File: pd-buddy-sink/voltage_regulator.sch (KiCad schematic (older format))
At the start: 5 parts, among them U1 AP2204R-3.3

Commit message: Added test points, replaced SW1 with R11
More test points will be needed for automated testing, so I've added the
first two I know of.

With firmware version 1.2.0+, there's not much reason to install SW1
anymore.  This commit replaces it with R11, an unpopulated resistor
footprint that does the same thing as bridging the two pins of SW1 used
to do, just in case an upgrade make the `boot` command stop working.
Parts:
- TP1, TP2: symbol TEST -> Test_Point
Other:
- moved on the sheet: TP1, TP2
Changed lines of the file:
@@
 $EndComp
 $Comp
-L TEST TP1
+L Test_Point TP1
 U 1 1 58FBCF4C
 P 4600 3600
@@
 $EndComp
 $Comp
-L TEST TP2
+L Test_Point TP2
 U 1 1 58FBD023
 P 4600 3800

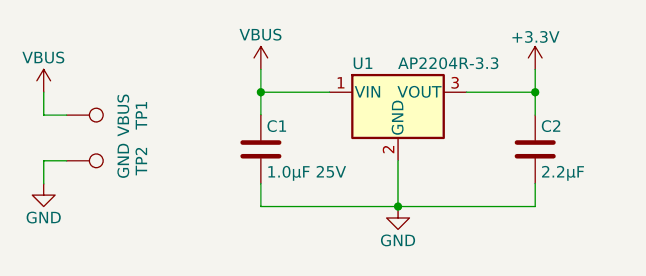
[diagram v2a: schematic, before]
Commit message: Update to KiCad 5.0 nightly
Hooray, new stuff!  The STM32 symbol is a reasonable size now!  We have
a sym-lib-table!  Everything is great, and I'm excited!

The board's a bit of a mess though, as the silkscreen needs to be laid
out nicely.  Oh well, details.
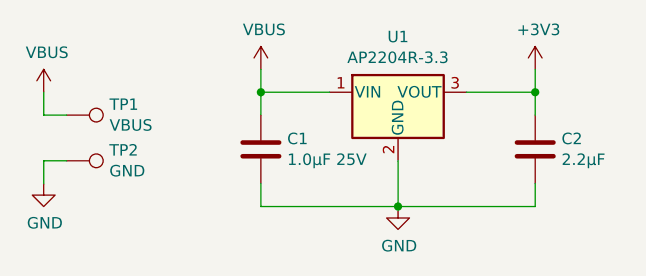
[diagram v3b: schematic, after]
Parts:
- removed C1: 1.0μF 25V, Capacitors_SMD:C_0603, symbol C
- removed C2: 2.2μF, Capacitors_SMD:C_0603, symbol C
- removed TP1: VBUS, Measurement_Points:Measurement_Point_Round-SMD-Pad_Small, symbol Test_Point
- removed TP2: GND, Measurement_Points:Measurement_Point_Round-SMD-Pad_Small, symbol Test_Point
- removed U1: AP2204R-3.3, TO_SOT_Packages_SMD:SOT-89-3, symbol AP2204R-3.3
- added C1: 1.0μF 25V, Capacitor_SMD:C_0603_1608Metric, symbol Device:C
- added C2: 2.2μF, Capacitor_SMD:C_0603_1608Metric, symbol Device:C
- added TP1: VBUS, TestPoint:TestPoint_Pad_D1.5mm, symbol Connector:Test_Point
- added TP2: GND, TestPoint:TestPoint_Pad_D1.5mm, symbol Connector:Test_Point
- added U1: AP2204R-3.3, Package_TO_SOT_SMD:SOT-89-3, symbol Regulator_Linear:AP2204R-3.3
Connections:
- net +3V3: now also C2.1, U1.3 (VOUT)
- net GND: now also C1.2, C2.2, TP2.1, U1.2 (GND)
- net VBUS: now also C1.1, TP1.1, U1.1 (VIN)
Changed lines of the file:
@@
-EESchema Schematic File Version 2
-LIBS:power
-LIBS:device
-LIBS:transistors
-LIBS:conn
-LIBS:linear
-LIBS:regul
-LIBS:74xx
-LIBS:cmos4000
-LIBS:adc-dac
-LIBS:memory
-LIBS:xilinx
-LIBS:microcontrollers
-LIBS:dsp
-LIBS:microchip
-LIBS:analog_switches
-LIBS:motorola
-LIBS:texas
-LIBS:intel
-LIBS:audio
-LIBS:interface
-LIBS:digital-audio
-LIBS:philips
-LIBS:display
-LIBS:cypress
-LIBS:siliconi
-LIBS:opto
-LIBS:atmel
-LIBS:contrib
-LIBS:valves
-LIBS:74xgxx
-LIBS:ac-dc
-LIBS:actel
-LIBS:allegro
-LIBS:Altera
-LIBS:analog_devices
-LIBS:battery_management
-LIBS:bbd
-LIBS:brooktre
-LIBS:cmos_ieee
-LIBS:dc-dc
-LIBS:diode
-LIBS:elec-unifil
-LIBS:ESD_Protection
-LIBS:ftdi
-LIBS:gennum
-LIBS:hc11
-LIBS:ir
-LIBS:Lattice
-LIBS:maxim
-LIBS:mechanical
-LIBS:microchip_dspic33dsc
-LIBS:microchip_pic10mcu
-LIBS:microchip_pic12mcu
-LIBS:microchip_pic16mcu
-LIBS:microchip_pic18mcu
-LIBS:microchip_pic32mcu
-LIBS:motor_drivers
-LIBS:motors
-LIBS:msp430
-LIBS:nordicsemi
-LIBS:nxp_armmcu
-LIBS:onsemi
-LIBS:Oscillators
-LIBS:powerint
-LIBS:Power_Management
-LIBS:pspice
-LIBS:references
-LIBS:relays
-LIBS:rfcom
-LIBS:sensors
-LIBS:silabs
-LIBS:stm32
-LIBS:stm8
-LIBS:supertex
-LIBS:switches
-LIBS:transf
-LIBS:ttl_ieee
-LIBS:video
-LIBS:wiznet
-LIBS:Worldsemi
-LIBS:Xicor
-LIBS:zetex
-LIBS:Zilog
-LIBS:pd-buddy
-LIBS:graphic_symbols
+EESchema Schematic File Version 4
 LIBS:pd-buddy-sink-cache
-EELAYER 25 0
+EELAYER 26 0
 EELAYER END
 $Descr USLetter 11000 8500
@@
 $EndDescr
 Wire Wire Line
-	5450 3400 5450 3600
+	5450 3400 5450 3500
 Connection ~ 6050 4000
 Wire Wire Line
 	5450 3900 5450 4000
 Wire Wire Line
-	5450 4000 6650 4000
+	5450 4000 6050 4000
 Wire Wire Line
 	6650 4000 6650 3900
 Wire Wire Line
-	6650 3400 6650 3600
-$Comp
-L C C2
-U 1 1 588FA3E5
-P 6650 3750
-F 0 "C2" H 6675 3850 50  0000 L CNN
-F 1 "2.2μF" H 6675 3650 50  0000 L CNN
-F 2 "Capacitors_SMD:C_0603" H 6688 3600 50  0001 C CNN
-F 3 "" H 6650 3750 50  0000 C CNN
-	1    6650 3750
-	1    0    0    -1
-$EndComp
-$Comp
-L C C1
-U 1 1 588FA3EC
-P 5450 3750
-F 0 "C1" H 5475 3850 50  0000 L CNN
-F 1 "1.0μF 25V" H 5475 3650 50  0000 L CNN
-F 2 "Capacitors_SMD:C_0603" H 5488 3600 50  0001 C CNN
-F 3 "" H 5450 3750 50  0000 C CNN
-	1    5450 3750
-	1    0    0    -1
-$EndComp
+	6650 3400 6650 3500
 Wire Wire Line
 	6050 3800 6050 4000
@@
 Wire Wire Line
 	5450 3500 5750 3500
-$Comp
-L GND #PWR03
-U 1 1 588FA3F6
-P 6050 4000
-F 0 "#PWR03" H 6050 3750 50  0001 C CNN
-F 1 "GND" H 6050 3850 50  0000 C CNN
-F 2 "" H 6050 4000 50  0000 C CNN
-F 3 "" H 6050 4000 50  0000 C CNN
-	1    6050 4000
-	1    0    0    -1
-$EndComp
-$Comp
-L +3.3V #PWR04
-U 1 1 588FA3FC
-P 6650 3400
-F 0 "#PWR04" H 6650 3250 50  0001 C CNN
-F 1 "+3.3V" H 6650 3540 50  0000 C CNN
-F 2 "" H 6650 3400 50  0000 C CNN
-F 3 "" H 6650 3400 50  0000 C CNN
-	1    6650 3400
-	1    0    0    -1
-$EndComp
-$Comp
-L GND #PWR05
-U 1 1 58FBCEDB
-P 4500 3900
-F 0 "#PWR05" H 4500 3650 50  0001 C CNN
-F 1 "GND" H 4500 3750 50  0000 C CNN
-F 2 "" H 4500 3900 50  0000 C CNN
-F 3 "" H 4500 3900 50  0000 C CNN
-	1    4500 3900
-	1    0    0    -1
-$EndComp
-$Comp
-L Test_Point TP1
-U 1 1 58FBCF4C
-P 4600 3600
-F 0 "TP1" H 4600 3900 50  0000 C BNN
-F 1 "VBUS" H 4600 3850 50  0000 C CNN
-F 2 "Measurement_Points:Measurement_Point_Round-SMD-Pad_Small" H 4600 3600 50  0001 C CNN
-F 3 "" H 4600 3600 50  0001 C CNN
-	1    4600 3600
-	0    1    1    0
-$EndComp
-$Comp
-L Test_Point TP2
-U 1 1 58FBD023
-P 4600 3800
-F 0 "TP2" H 4600 4100 50  0000 C BNN
-F 1 "GND" H 4600 4050 50  0000 C CNN
-F 2 "Measurement_Points:Measurement_Point_Round-SMD-Pad_Small" H 4600 3800 50  0001 C CNN
-F 3 "" H 4600 3800 50  0001 C CNN
-	1    4600 3800
-	0    1    1    0
-$EndComp
 Wire Wire Line
 	4600 3600 4500 3600
@@
 Wire Wire Line
 	4500 3800 4500 3900
+Connection ~ 5450 3500
+Connection ~ 6650 3500
+Wire Wire Line
+	6050 4000 6650 4000
+Wire Wire Line
+	5450 3500 5450 3600
+Wire Wire Line
+	6650 3500 6650 3600
 $Comp
-L VBUS #PWR06
-U 1 1 592B5581
+L Connector:Test_Point TP1
+U 1 1 5A9A03D6
+P 4600 3600
+F 0 "TP1" V 4554 3788 50  0000 L CNN
+F 1 "VBUS" V 4645 3788 50  0000 L CNN
+F 2 "TestPoint:TestPoint_Pad_D1.5mm" H 4800 3600 50  0001 C CNN
+F 3 "~" H 4800 3600 50  0001 C CNN
+	1    4600 3600
+	0    1    1    0
+$EndComp
+$Comp
+L Connector:Test_Point TP2
+U 1 1 5A9A08D7
+P 4600 3800
+F 0 "TP2" V 4554 3987 50  0000 L CNN
+F 1 "GND" V 4645 3987 50  0000 L CNN
+F 2 "TestPoint:TestPoint_Pad_D1.5mm" H 4800 3800 50  0001 C CNN
+F 3 "~" H 4800 3800 50  0001 C CNN
+	1    4600 3800
+	0    1    1    0
+$EndComp
+$Comp
+L Device:C C1
+U 1 1 5A9A0AA0
+P 5450 3750
+F 0 "C1" H 5565 3796 50  0000 L CNN
+F 1 "1.0μF 25V" H 5565 3705 50  0000 L CNN
+F 2 "Capacitor_SMD:C_0603_1608Metric" H 5488 3600 50  0001 C CNN
+F 3 "~" H 5450 3750 50  0001 C CNN
+	1    5450 3750
+	1    0    0    -1
+$EndComp
+$Comp
+L Device:C C2
+U 1 1 5A9A0FC3
+P 6650 3750
+F 0 "C2" H 6765 3796 50  0000 L CNN
+F 1 "2.2μF" H 6765 3705 50  0000 L CNN
+F 2 "Capacitor_SMD:C_0603_1608Metric" H 6688 3600 50  0001 C CNN
+F 3 "~" H 6650 3750 50  0001 C CNN
+	1    6650 3750
+	1    0    0    -1
+$EndComp
+$Comp
+L power:VBUS #PWR0103
+U 1 1 5A9A116F
+P 4500 3500
+F 0 "#PWR0103" H 4500 3350 50  0001 C CNN
+F 1 "VBUS" H 4515 3673 50  0000 C CNN
+F 2 "" H 4500 3500 50  0001 C CNN
+F 3 "" H 4500 3500 50  0001 C CNN
+	1    4500 3500
+	1    0    0    -1
+$EndComp
+$Comp
+L power:VBUS #PWR0104
+U 1 1 5A9A11B0
 P 5450 3400
-F 0 "#PWR06" H 5450 3250 50  0001 C CNN
-F 1 "VBUS" H 5450 3550 50  0000 C CNN
+F 0 "#PWR0104" H 5450 3250 50  0001 C CNN
+F 1 "VBUS" H 5465 3573 50  0000 C CNN
 F 2 "" H 5450 3400 50  0001 C CNN
 F 3 "" H 5450 3400 50  0001 C CNN
@@
 $EndComp
 $Comp
-L VBUS #PWR07
-U 1 1 592B55C7
-P 4500 3500
-F 0 "#PWR07" H 4500 3350 50  0001 C CNN
-F 1 "VBUS" H 4500 3650 50  0000 C CNN
-F 2 "" H 4500 3500 50  0001 C CNN
-F 3 "" H 4500 3500 50  0001 C CNN
-	1    4500 3500
+L power:GND #PWR0105
+U 1 1 5A9A124A
+P 4500 3900
+F 0 "#PWR0105" H 4500 3650 50  0001 C CNN
+F 1 "GND" H 4505 3727 50  0000 C CNN
+F 2 "" H 4500 3900 50  0001 C CNN
+F 3 "" H 4500 3900 50  0001 C CNN
+	1    4500 3900
 	1    0    0    -1
 $EndComp
 $Comp
-L AP2204R-3.3 U1
-U 1 1 5961518D
+L power:GND #PWR0106
+U 1 1 5A9A1285
+P 6050 4000
+F 0 "#PWR0106" H 6050 3750 50  0001 C CNN
+F 1 "GND" H 6055 3827 50  0000 C CNN
+F 2 "" H 6050 4000 50  0001 C CNN
+F 3 "" H 6050 4000 50  0001 C CNN
+	1    6050 4000
+	1    0    0    -1
+$EndComp
+$Comp
+L power:+3V3 #PWR0107
+U 1 1 5A9A1474
+P 6650 3400
+F 0 "#PWR0107" H 6650 3250 50  0001 C CNN
+F 1 "+3V3" H 6665 3573 50  0000 C CNN
+F 2 "" H 6650 3400 50  0001 C CNN
+F 3 "" H 6650 3400 50  0001 C CNN
+	1    6650 3400
+	1    0    0    -1
+$EndComp
+$Comp
+L Regulator_Linear:AP2204R-3.3 U1
+U 1 1 5A9A1618
 P 6050 3500
-F 0 "U1" H 5850 3625 50  0000 L CNN
-F 1 "AP2204R-3.3" H 6050 3625 50  0000 L CNN
-F 2 "TO_SOT_Packages_SMD:SOT-89-3" H 6050 3725 50  0001 C CNN
-F 3 "" H 6050 3500 50  0001 C CNN
+F 0 "U1" H 6050 3742 50  0000 C CNN
+F 1 "AP2204R-3.3" H 6050 3651 50  0000 C CNN
+F 2 "Package_TO_SOT_SMD:SOT-89-3" H 6050 3725 50  0001 C CNN
+F 3 "https://www.diodes.com/assets/Datasheets/AP2204.pdf" H 6050 3500 50  0001 C CNN
 	1    6050 3500
 	1    0    0    -1
 $EndComp
-Connection ~ 5450 3500
-Connection ~ 6650 3500
 $EndSCHEMATC
